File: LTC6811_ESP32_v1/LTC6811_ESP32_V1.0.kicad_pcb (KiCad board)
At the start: 2 copper layers, 130 x 90 mm, 266 parts, among them J1 12/24V, J10 Hole /NC, J11 Hole /NC, J12 Hole /NC, J13 B7B-XH-A, J14 B7B-XH-A, J15 PB MB, J2 OLED /NC, J3 CAN /NC, J4 USB, J5 UART /NC, J6 JTAG /NC, J7 Boot Option /NC, J8 SERIAL /NC, J9 GND, Q1 BSS138, Q10 TSM2323, Q11 TSM2323, Q12 TSM2323, Q13 TSM2323, Q14 TSM2323, Q2 NSV1C201MZ4, Q3 TSM2323, Q4 TSM2323, Q5 TSM2323, Q6 TSM2323, Q7 TSM2323, Q8 TSM2323, Q9 TSM2323, U1 TPS76350, U10 CP2104, U11 ISO1050DUBR, U12 LTC6811HG-1, U2 AMC1301 or AMC1302, U3 AMC1301, U4 SN6501DBV, U5 OPA2197IDR, U6 ISL28022, U7 TPS54160ADGQ, U8 ESP32-DevKitC V4, U9 LTC6820

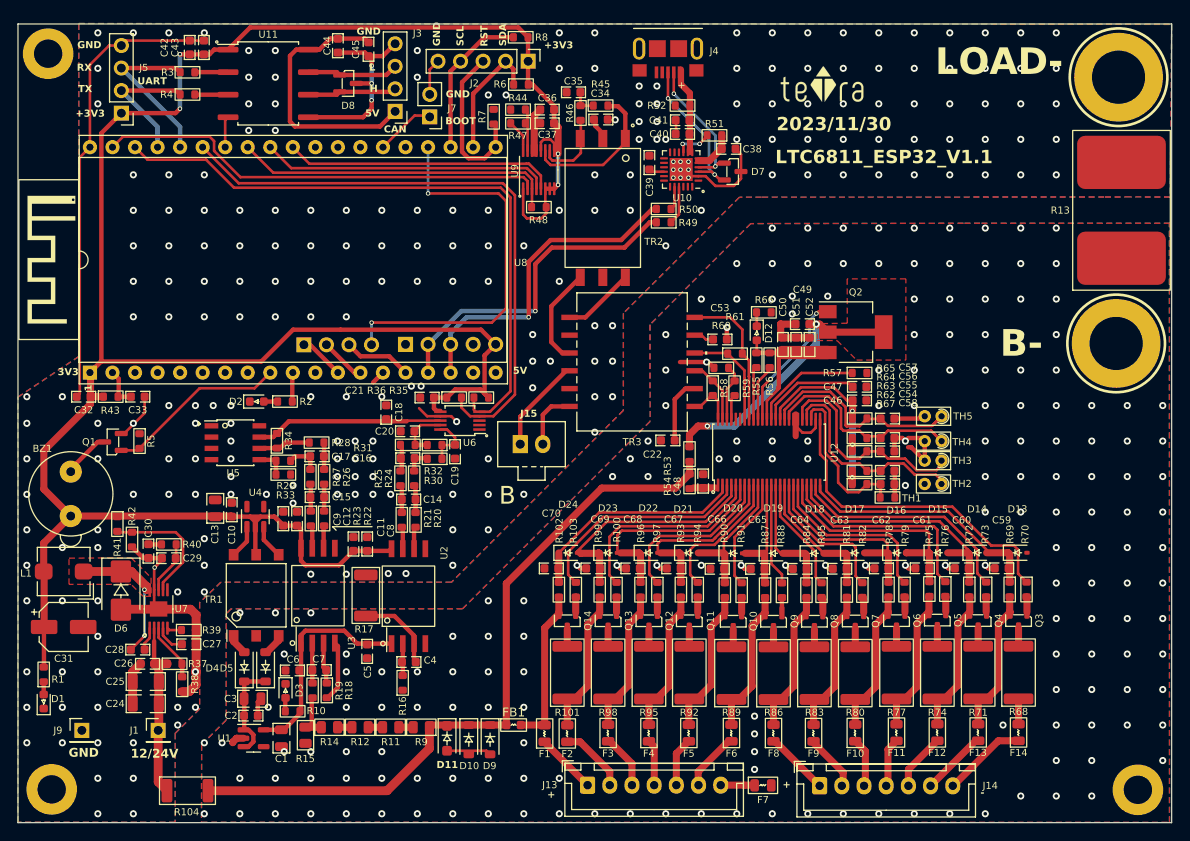
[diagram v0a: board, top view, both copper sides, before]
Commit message: Optimize Isolated Power Supply Circuit
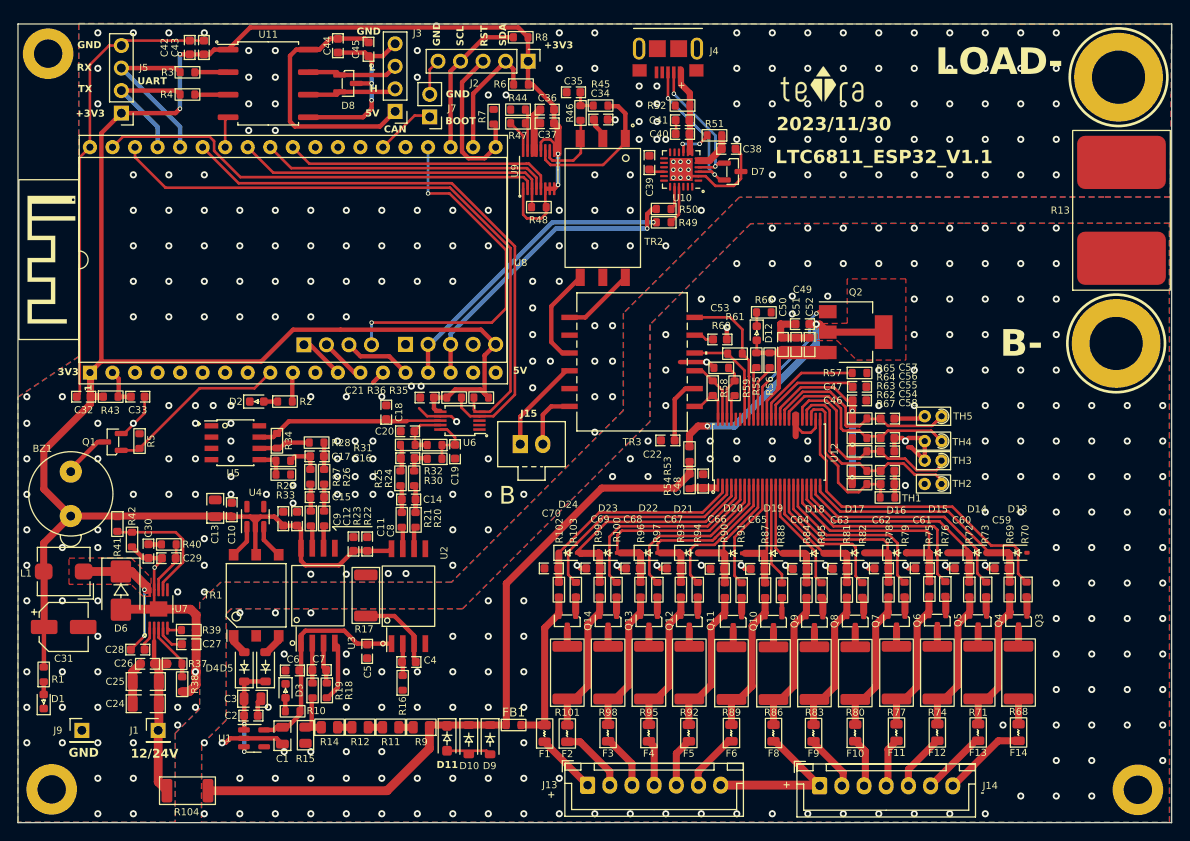
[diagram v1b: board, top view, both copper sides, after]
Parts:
- removed F7: MPZ2012S102ATD25, Fuse:Fuse_0805_2012Metric
- FB1: footprint Fuse:Fuse_0603_1608Metric -> Resistor_SMD:R_0603_1608Metric
- LOGO1: value teTra-LOGO -> teTra /NC
- moved C1 0.30 mm to (92.9, 130.7)
- moved U1 0.05 mm to (89.7, 131.0)
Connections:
- J13 pad 0: /LTC6811/C2_G -> /LTC6811/C6
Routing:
- net /LTC6811/C6: track 7.26 -> 18.4 mm
- net GND_PACK: track 65.5 -> 71.3 mm, vias 194 -> 191
- net /LTC6811/C2_G: track 3.80 -> 0.00 mm
- net /MCU/SDA: track 68.5 -> 65.1 mm
- net /MCU/MTDO: track 44.8 -> 41.5 mm
- net /MCU/RX_USB: track 37.7 -> 34.6 mm
- net /MCU/TX_USB: track 37.1 -> 34.3 mm
- net /MCU/SCL: track 72.6 -> 70.0 mm
- net Net-(D4-K): vias 0 -> 2
- net GND: vias 241 -> 244
